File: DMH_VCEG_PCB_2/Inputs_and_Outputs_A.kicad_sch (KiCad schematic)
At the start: 39 parts, among them J1 TS_Jack_6.35mm_Sw, J10 TS_Jack_6.35mm_Sw, J2 TS_Jack_6.35mm_Sw, J200 IDC_02x08, J21 Conn_01x10_PinHeader, J22 Conn_01x10_PinHeader, J23 Conn_01x10_PinHeader, J27 Conn_01x06_PinHeader, J3 TS_Jack_6.35mm_Sw, J4 TS_Jack_6.35mm_Sw, J5 TS_Jack_6.35mm_Sw, J6 TS_Jack_6.35mm_Sw, J7 TS_Jack_6.35mm_Sw, J8 TS_Jack_6.35mm_Sw, J9 TS_Jack_6.35mm_Sw, U21 TL074, U9 TL074

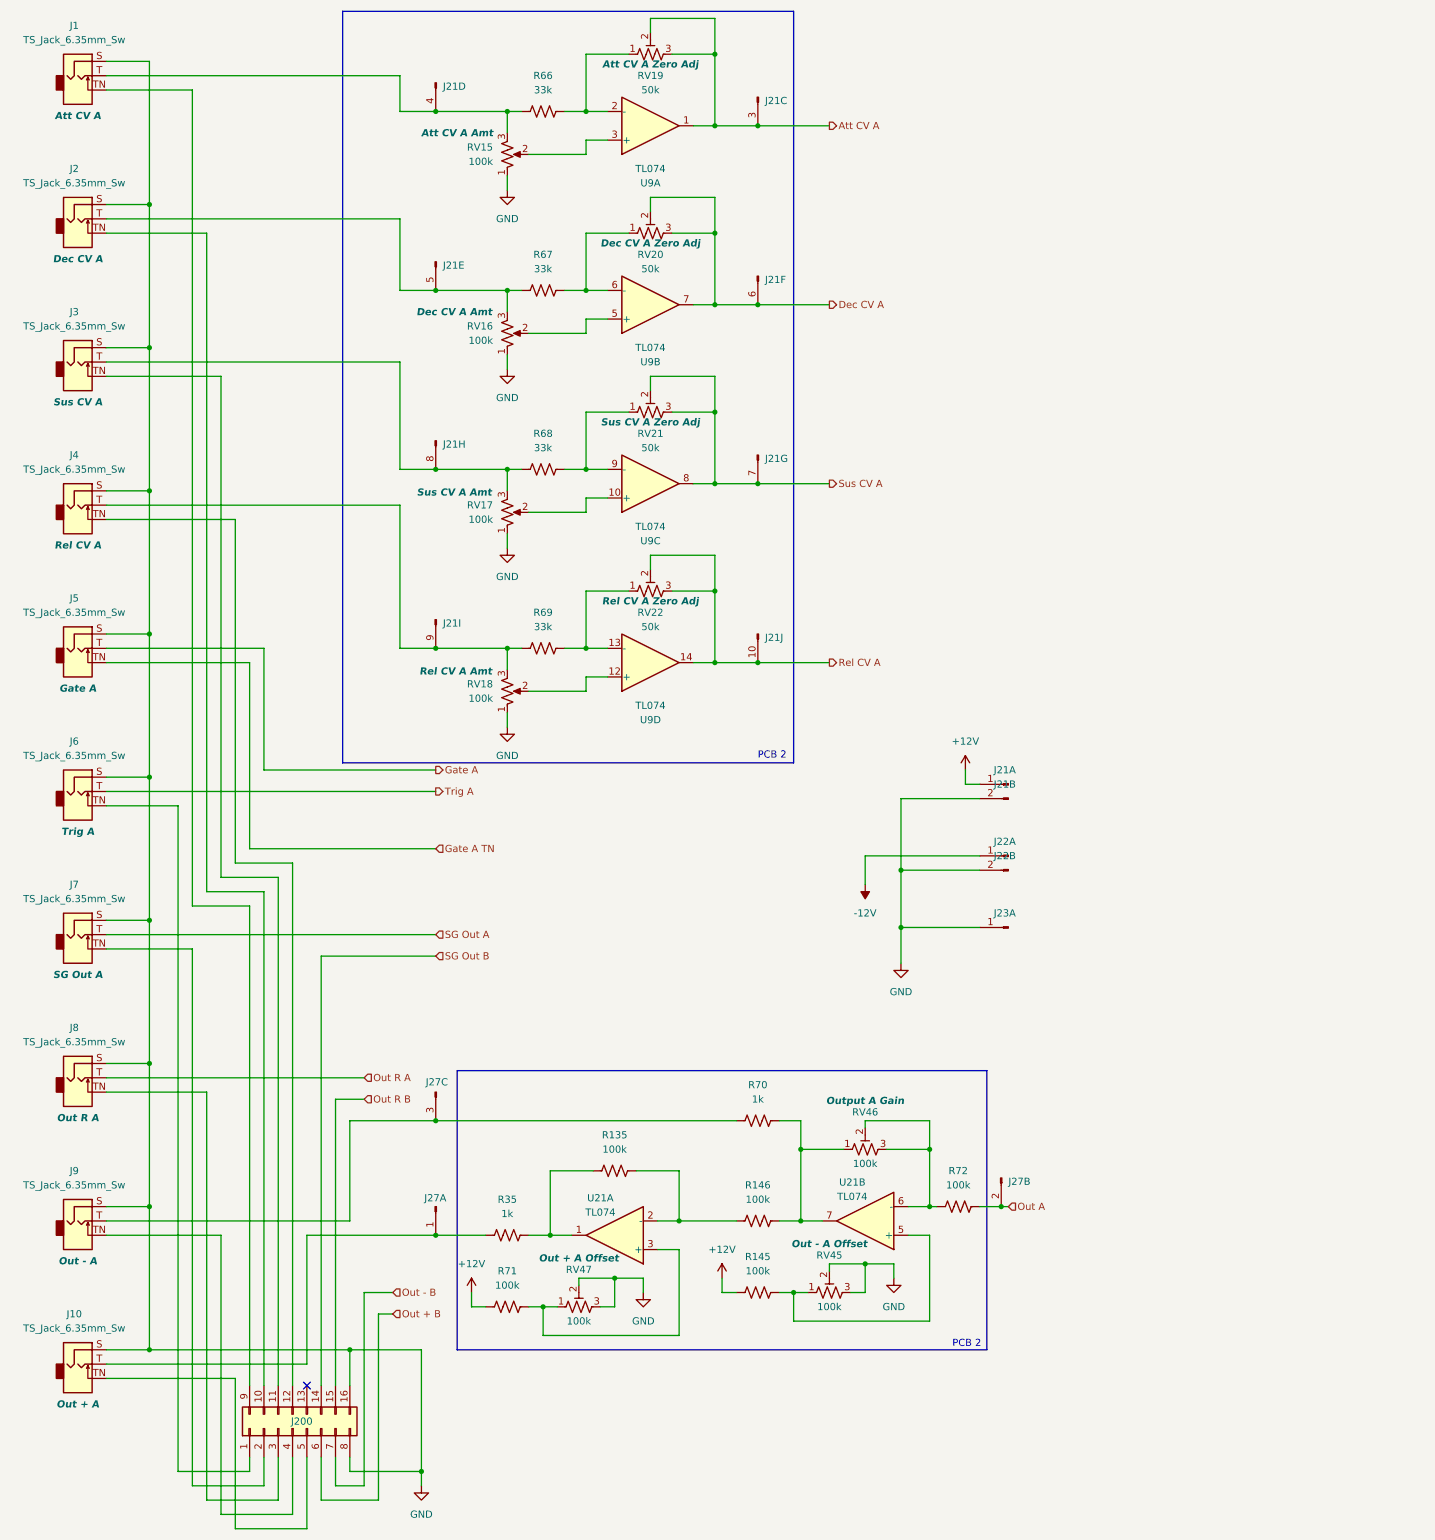
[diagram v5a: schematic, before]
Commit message: Synced PCB 2 project with PCB 1
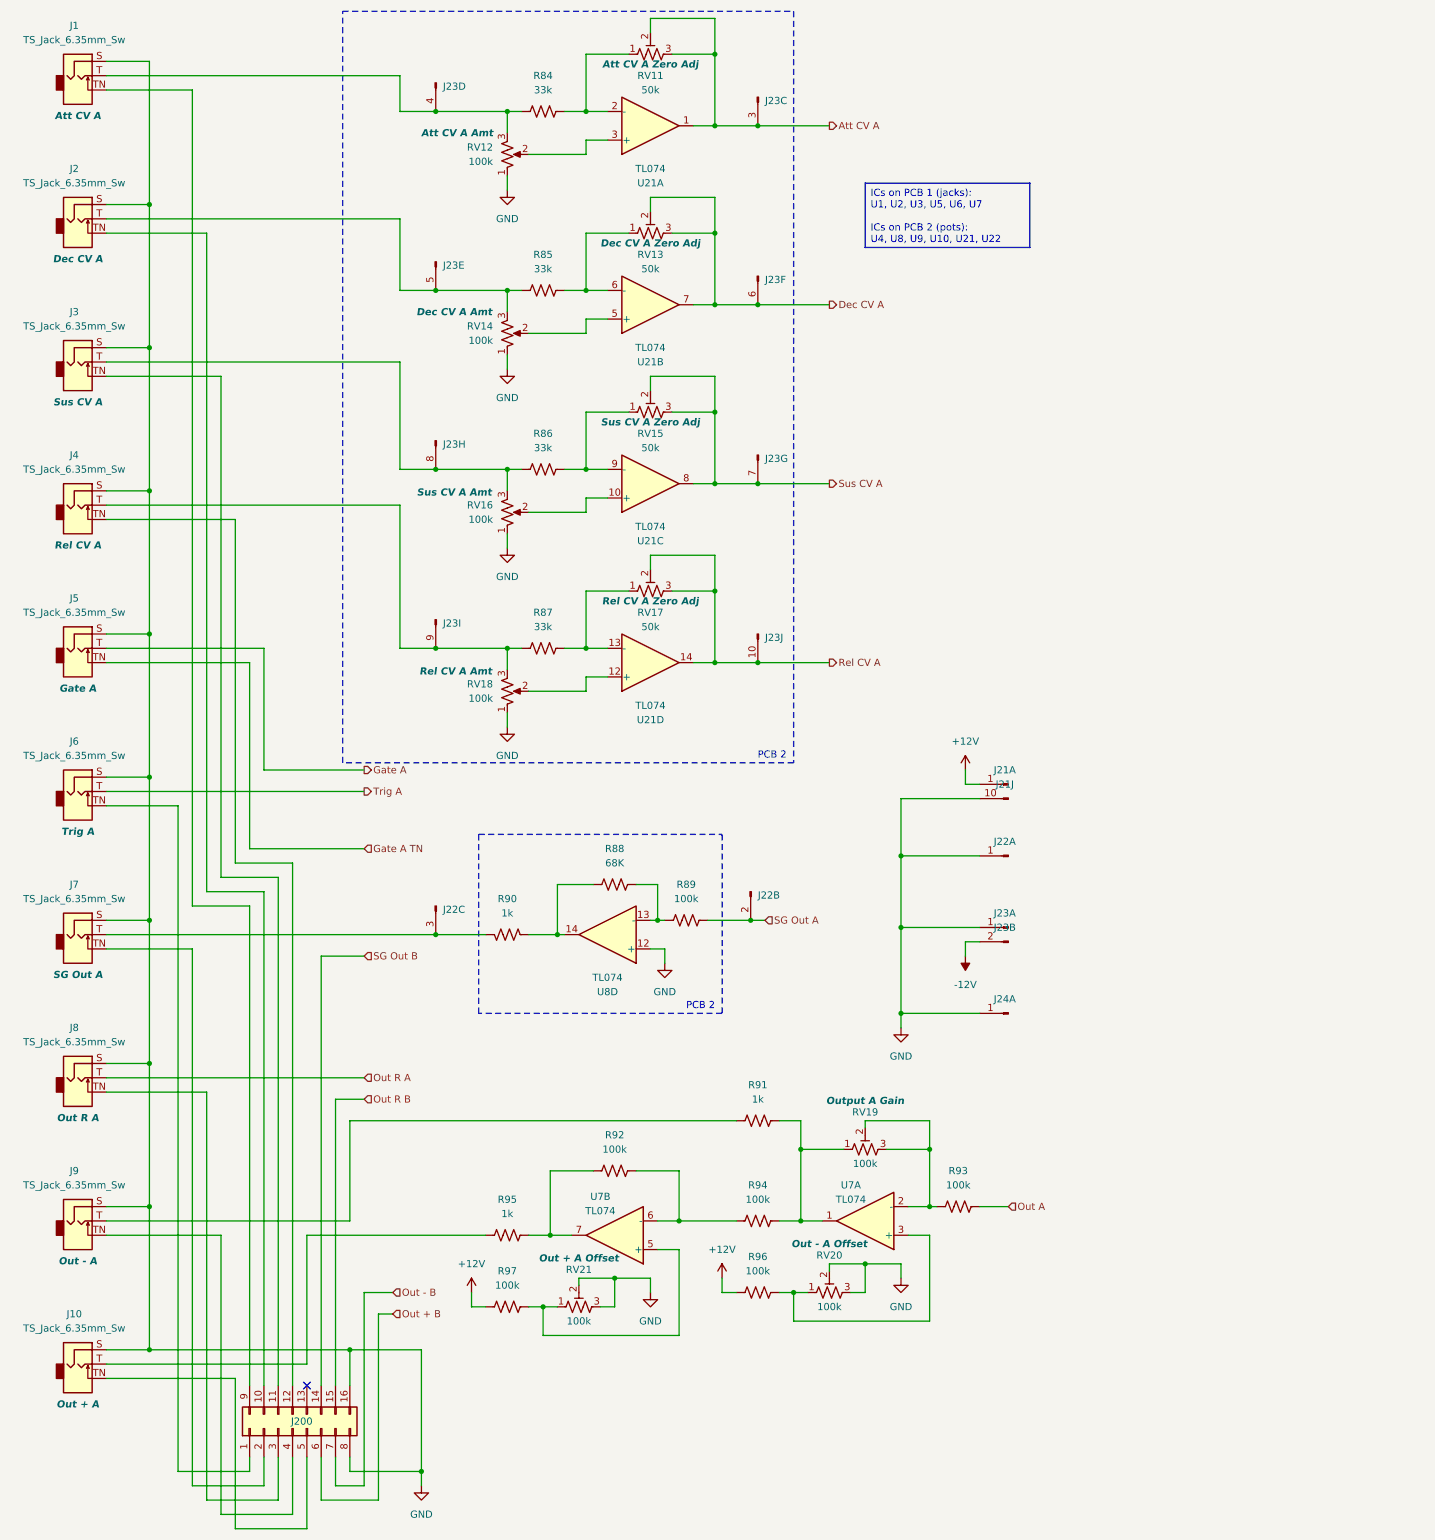
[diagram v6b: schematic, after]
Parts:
- removed J27: Conn_01x06_PinHeader, Connector_PinSocket_2.54mm:PinSocket_1x06_P2.54mm_Vertical, symbol SynthStuff:Conn_01x06_PinHeader
- removed R135, R146, R71: 100k, Resistor_THT:R_Axial_DIN0207_L6.3mm_D2.5mm_P7.62mm_Horizontal, symbol Device:R_US
- removed U21: TL074, symbol Amplifier_Operational:TL074
- added unit 2 of J22
- added unit 3 of J22
- added J24: Conn_01x06_PinHeader, Connector_PinHeader_2.54mm:PinHeader_1x06_P2.54mm_Vertical, symbol SynthStuff:Conn_01x06_PinHeader
- added R88: 68K, Resistor_THT:R_Axial_DIN0207_L6.3mm_D2.5mm_P7.62mm_Horizontal, symbol Device:R_US
- added R89, R92, R94, R97: 100k, Resistor_THT:R_Axial_DIN0207_L6.3mm_D2.5mm_P7.62mm_Horizontal, symbol Device:R_US
- added R90: 1k, Resistor_THT:R_Axial_DIN0207_L6.3mm_D2.5mm_P7.62mm_Horizontal, symbol Device:R_US
- added U7, U8: TL074, Package_DIP:DIP-14_W7.62mm_Socket, symbol Amplifier_Operational:TL074
- J21: footprint Connector_PinSocket_2.54mm:PinSocket_1x10_P2.54mm_Vertical -> Connector_PinHeader_2.54mm:PinHeader_1x10_P2.54mm_Vertical
- RV19: renamed from RV46; footprint Potentiometer_THT:Potentiometer_Bourns_3296X_Horizontal -> Potentiometer_THT:Potentiometer_Bourns_3296W_Vertical
- RV20: renamed from RV45; footprint Potentiometer_THT:Potentiometer_Bourns_3296X_Horizontal -> Potentiometer_THT:Potentiometer_Bourns_3296W_Vertical
- RV21: renamed from RV47; footprint Potentiometer_THT:Potentiometer_Bourns_3296X_Horizontal -> Potentiometer_THT:Potentiometer_Bourns_3296W_Vertical
- renumbered J21 to J23, J22 to J23, R66 to R84, R67 to R85, R68 to R86, R69 to R87, R70 to R91, R72 to R93, R35 to R95, R145 to R96, RV19 to RV11, RV15 to RV12, RV20 to RV13, RV16 to RV14, RV21 to RV15, RV17 to RV16, RV22 to RV17, U9 to U21
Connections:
- net +12V: now also R97.2
- net -12V: now also J23.2 (Pin_2); no longer J22.1 (Pin_1)
- net GND: now also J21.10 (Pin_10), J22.1 (Pin_1), J24.1 (Pin_1), U8.12 (+); no longer J21.2 (Pin_2), J23.2 (Pin_2)
- net SG Out A: now also J22.2 (Pin_2), R89.1; no longer J7.T
- net at R95.1: now also R92.2, U7.7
- net at R93.2, RV19.2, RV19.3: now also U7.2 (-)
- net at R96.1, RV20.1: now also U7.3 (+)
- net at RV21.1: now also R97.1, U7.5 (+)
- net at R91.1, RV19.1: now also R94.1, U7.1
- new net: J22.3 (Pin_3), J7.T, R90.1
- new net: R88.2, R90.2, U8.14
- new net: R88.1, R89.2, U8.13 (-)
- new net: R92.1, R94.2, U7.6 (-)
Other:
- moved on the sheet: J23B

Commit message: Started placement on PCB 2
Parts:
- J21: footprint Connector_PinHeader_2.54mm:PinHeader_1x10_P2.54mm_Vertical -> Connector_PinSocket_2.54mm:PinSocket_1x10_P2.54mm_Vertical
- J24: footprint Connector_PinHeader_2.54mm:PinHeader_1x06_P2.54mm_Vertical -> Connector_PinSocket_2.54mm:PinSocket_1x06_P2.54mm_Vertical
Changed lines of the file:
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@@
 			)
 		)
-		(property "Footprint" "Connector_PinHeader_2.54mm:PinHeader_1x10_P2.54mm_Vertical"
+		(property "Footprint" "Connector_PinSocket_2.54mm:PinSocket_1x10_P2.54mm_Vertical"
 			(at 190.5 151.13 0)
 			(effects
@@
 			)
 		)
-		(property "Footprint" "Connector_PinHeader_2.54mm:PinHeader_1x10_P2.54mm_Vertical"
+		(property "Footprint" "Connector_PinSocket_2.54mm:PinSocket_1x10_P2.54mm_Vertical"
 			(at 190.5 153.67 0)
 			(effects
@@
 			)
 		)
-		(property "Footprint" "Connector_PinHeader_2.54mm:PinHeader_1x06_P2.54mm_Vertical"
+		(property "Footprint" "Connector_PinSocket_2.54mm:PinSocket_1x06_P2.54mm_Vertical"
 			(at 190.5 191.77 0)
 			(effects

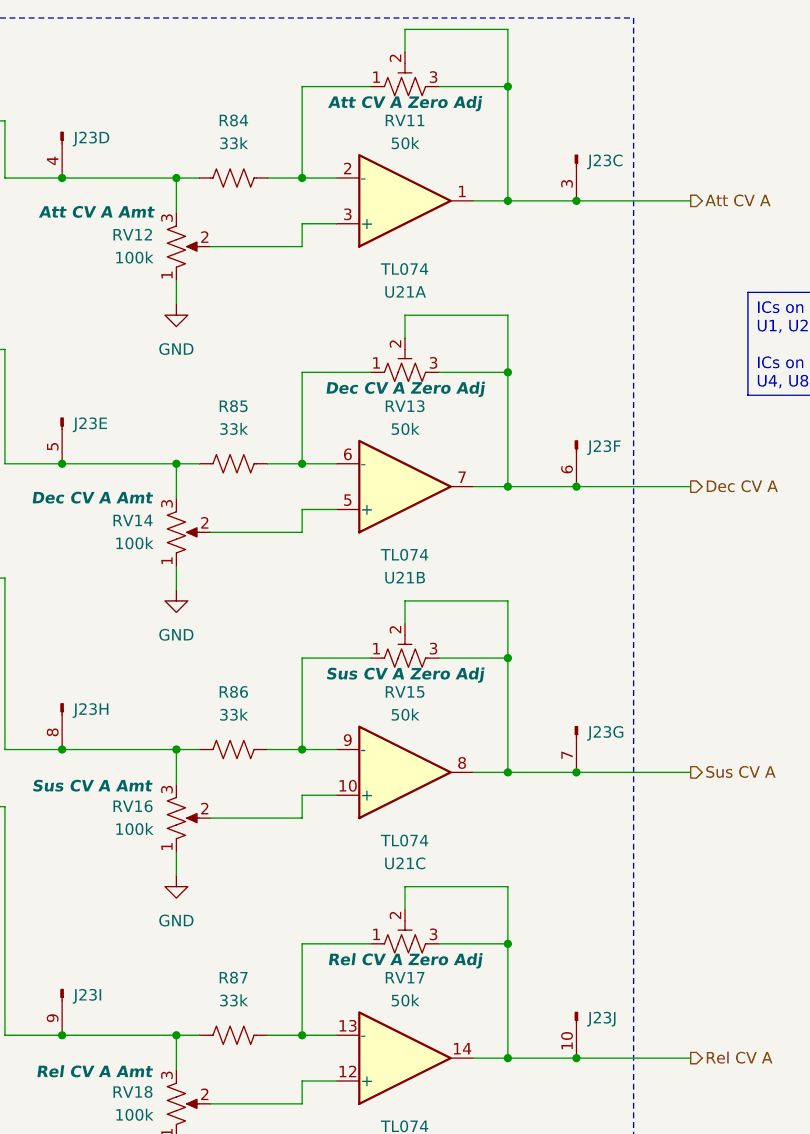
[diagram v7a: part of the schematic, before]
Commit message: PCB 2 placement in progress
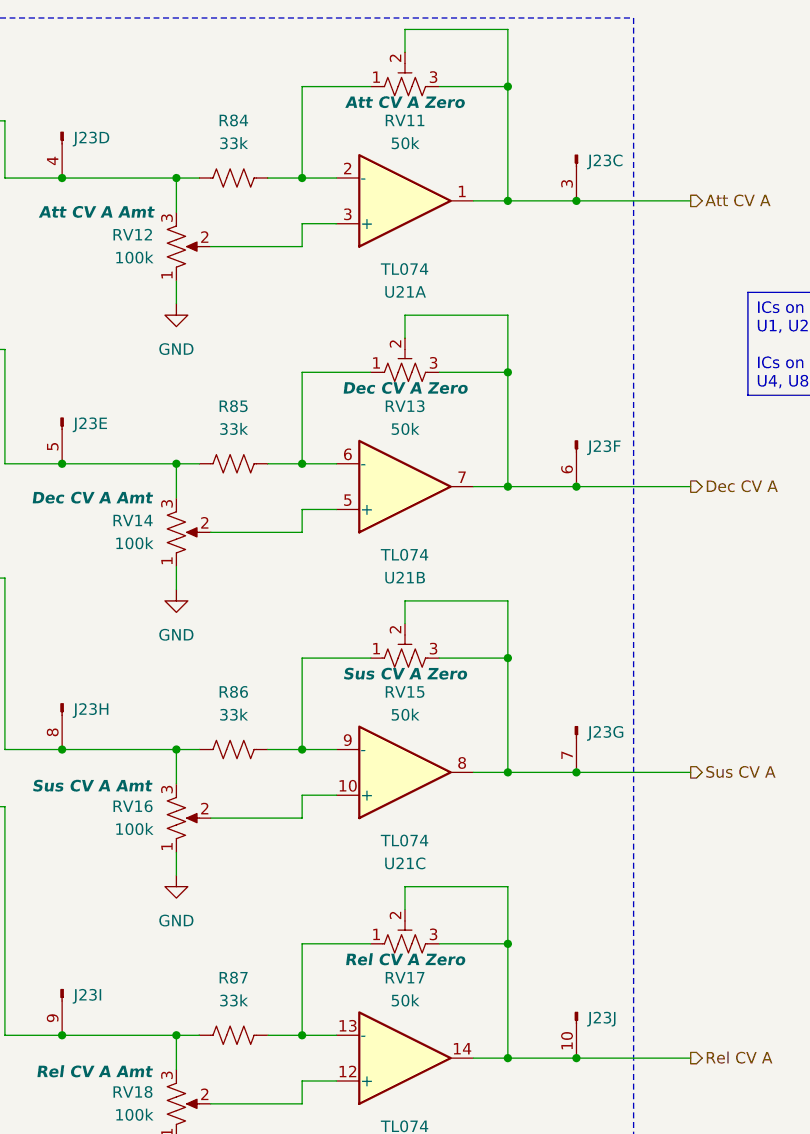
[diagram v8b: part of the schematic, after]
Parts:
- RV11: Function Att CV A Zero Adj -> Att CV A Zero
- RV13: Function Dec CV A Zero Adj -> Dec CV A Zero
- RV15: Function Sus CV A Zero Adj -> Sus CV A Zero
- RV17: Function Rel CV A Zero Adj -> Rel CV A Zero
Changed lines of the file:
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@@
 			)
 		)
-		(property "Function" "Sus CV A Zero Adj"
+		(property "Function" "Sus CV A Zero"
 			(at 127 86.868 90)
 			(effects
@@
 			)
 		)
-		(property "Function" "Dec CV A Zero Adj"
+		(property "Function" "Dec CV A Zero"
 			(at 127 55.118 90)
 			(effects
@@
 			)
 		)
-		(property "Function" "Rel CV A Zero Adj"
+		(property "Function" "Rel CV A Zero"
 			(at 127 118.618 90)
 			(effects
@@
 			)
 		)
-		(property "Function" "Att CV A Zero Adj"
+		(property "Function" "Att CV A Zero"
 			(at 127 23.368 90)
 			(effects
